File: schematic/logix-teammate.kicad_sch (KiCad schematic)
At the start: 28 parts

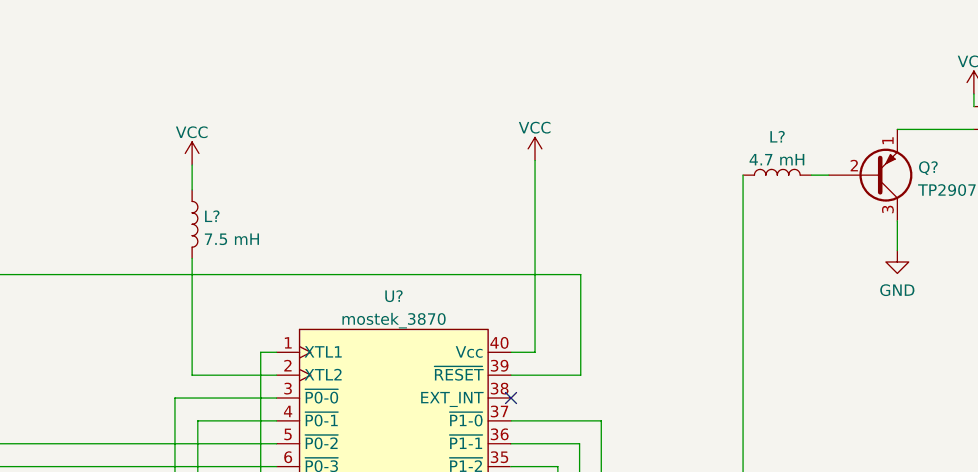
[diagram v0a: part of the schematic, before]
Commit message: corrected resistors
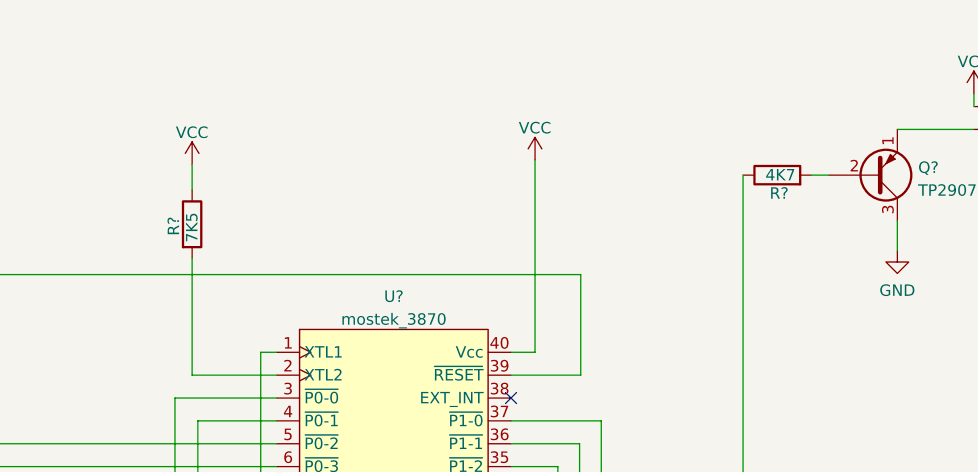
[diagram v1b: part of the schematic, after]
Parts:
- removed L?: 7.5 mH, symbol Device:L
- removed L?: 4.7 mH, symbol Device:L
- added R?: 7K5, symbol Device:R
- added R?: 4K7, symbol Device:R
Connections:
- net VCC: now also R?.1
- net at Q?.2 (B): now also R?.2
- net at U?.2 (XTL2): now also R?.2
- net at U?.33 (~{P5-0}): now also R?.1
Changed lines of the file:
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@@
     (pin "3")
+  )
+  (symbol (lib_id "Device:R") (at 88.9 37.592 0) (unit 1)
+    (in_bom yes) (on_board yes)
+    (property "Reference" "R?" (id 0) (at 86.868 38.862 90)
+      (effects (font (size 1.27 1.27)) (justify left))
+    )
+    (property "Value" "7K5" (id 1) (at 88.9 39.624 90)
+      (effects (font (size 1.27 1.27)) (justify left))
+    )
+    (property "Footprint" "" (id 2) (at 87.122 37.592 90)
+      (effects (font (size 1.27 1.27)) hide)
+    )
+    (property "Datasheet" "~" (id 3) (at 88.9 37.592 0)
+      (effects (font (size 1.27 1.27)) hide)
+    )
+    (pin "1")
+    (pin "2")
   )
   (symbol (lib_id "Simulation_SPICE:DIODE") (at 28.702 21.336 0) (unit 1)
@@
     (pin "1")
   )
-  (symbol (lib_id "Device:L") (at 88.9 37.592 0) (unit 1)
-    (in_bom yes) (on_board yes) (fields_autoplaced)
-    (property "Reference" "L?" (id 0) (at 90.17 36.7573 0)
-      (effects (font (size 1.27 1.27)) (justify left))
-    )
-    (property "Value" "7.5 mH" (id 1) (at 90.17 39.2942 0)
-      (effects (font (size 1.27 1.27)) (justify left))
-    )
-    (property "Footprint" "" (id 2) (at 88.9 37.592 0)
-      (effects (font (size 1.27 1.27)) hide)
-    )
-    (property "Datasheet" "~" (id 3) (at 88.9 37.592 0)
-      (effects (font (size 1.27 1.27)) hide)
-    )
-    (pin "1")
-    (pin "2")
-  )
-  (symbol (lib_id "Device:L") (at 153.924 32.131 90) (unit 1)
-    (in_bom yes) (on_board yes) (fields_autoplaced)
-    (property "Reference" "L?" (id 0) (at 153.924 27.9232 90))
-    (property "Value" "4.7 mH" (id 1) (at 153.924 30.4601 90))
-    (property "Footprint" "" (id 2) (at 153.924 32.131 0)
+  (symbol (lib_id "Device:R") (at 153.924 32.131 90) (unit 1)
+    (in_bom yes) (on_board yes)
+    (property "Reference" "R?" (id 0) (at 155.194 34.163 90)
+      (effects (font (size 1.27 1.27)) (justify left))
+    )
+    (property "Value" "4K7" (id 1) (at 155.956 32.131 90)
+      (effects (font (size 1.27 1.27)) (justify left))
+    )
+    (property "Footprint" "" (id 2) (at 153.924 33.909 90)
       (effects (font (size 1.27 1.27)) hide)
     )
@@
       (reference "D?") (unit 1) (value "LED3") (footprint "")
     )
-    (path "/b9464cb5-be60-4318-8cf9-72da0420fd2d"
-      (reference "L?") (unit 1) (value "7.5 mH") (footprint "")
-    )
-    (path "/c63b8724-5fa8-402a-9aaf-6c3f5c788b0e"
-      (reference "L?") (unit 1) (value "4.7 mH") (footprint "")
-    )
     (path "/d2d8d5bc-d157-4dc7-8a38-0eb37d571cc5"
       (reference "LS?") (unit 1) (value "8Ω") (footprint "")
@@
       (reference "R?") (unit 1) (value "1K5") (footprint "")
     )
+    (path "/3f472c77-a5d2-4b6b-9823-a0f6ca014294"
+      (reference "R?") (unit 1) (value "7K5") (footprint "")
+    )
     (path "/4e283cb3-1a3a-4878-86b7-4bf04f7ee0aa"
       (reference "R?") (unit 1) (value "1K5") (footprint "")
@@
       (reference "R?") (unit 1) (value "1K") (footprint "")
     )
+    (path "/cf9a9387-64b3-4fb2-b3b7-204c4f9a1e23"
+      (reference "R?") (unit 1) (value "4K7") (footprint "")
+    )
     (path "/d844314d-080e-4756-9dbe-bc6b67245e8d"

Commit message: update schematics
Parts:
- gave numbers to parts that had none: 28
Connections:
- net VCC: now also U2.18 (VCC)
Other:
- sheet TEAMMATE Keypad renamed Keypad

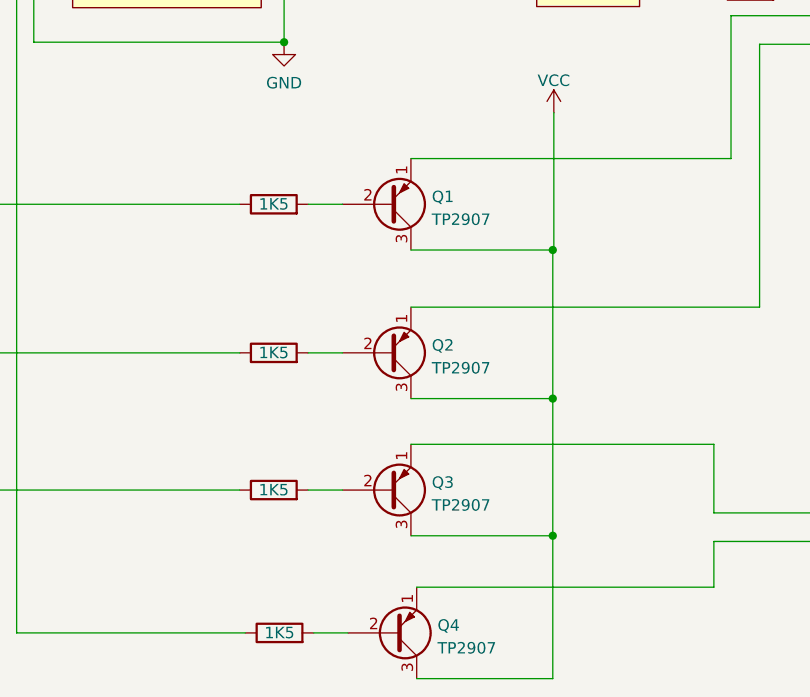
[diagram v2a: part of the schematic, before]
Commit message: corrected transitor polarity
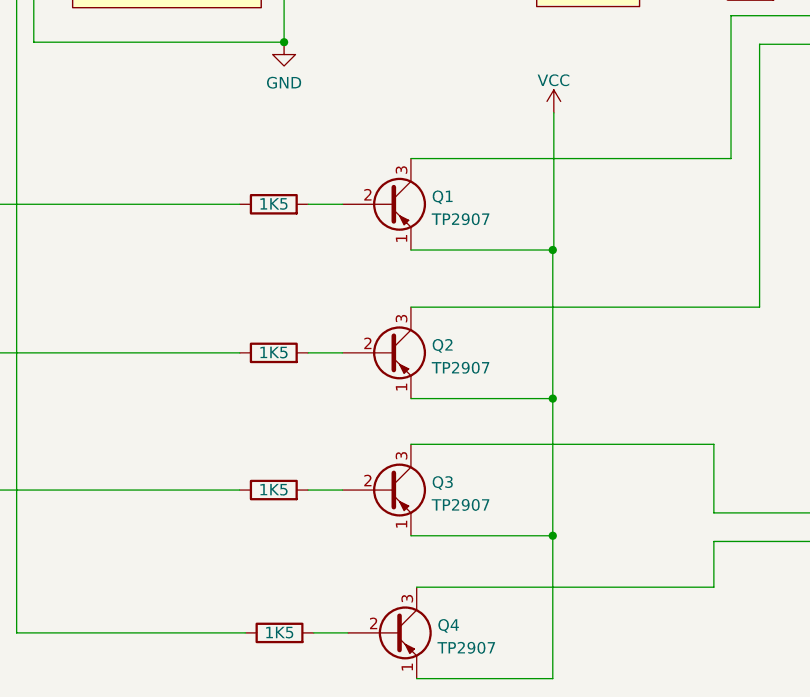
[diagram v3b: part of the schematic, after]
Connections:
- net LED Array/A1: now also Q2.3 (C); no longer Q2.1 (E)
- net LED Array/A2: now also Q1.3 (C); no longer Q1.1 (E)
- net VCC: now also Q1.1 (E), Q2.1 (E), Q3.1 (E), Q4.1 (E); no longer Q1.3 (C), Q2.3 (C), Q3.3 (C), Q4.3 (C)
- net at U4.14 (CA): now also Q4.3 (C); no longer Q4.1 (E)
- net at U3.3 (CA): now also Q3.3 (C); no longer Q3.1 (E)
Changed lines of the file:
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@@
     (pin "2")
   )
-  (symbol (lib_id "Transistor_BJT:2N3906") (at 136.525 171.45 0) (mirror x) (unit 1)
+  (symbol (lib_id "Transistor_BJT:2N3906") (at 136.525 171.45 0) (unit 1)
     (in_bom yes) (on_board yes) (fields_autoplaced)
     (property "Reference" "Q4" (id 0) (at 141.3764 170.6153 0)
@@
       (effects (font (size 1.27 1.27)) (justify left))
     )
-    (property "Footprint" "Package_TO_SOT_THT:TO-92_Inline" (id 2) (at 141.605 169.545 0)
+    (property "Footprint" "Package_TO_SOT_THT:TO-92_Inline" (id 2) (at 141.605 173.355 0)
       (effects (font (size 1.27 1.27) italic) (justify left) hide)
     )
@@
     (pin "2")
   )
-  (symbol (lib_id "Transistor_BJT:2N3906") (at 135.89 140.335 0) (mirror x) (unit 1)
+  (symbol (lib_id "Transistor_BJT:2N3906") (at 135.89 140.335 0) (unit 1)
     (in_bom yes) (on_board yes) (fields_autoplaced)
     (property "Reference" "Q2" (id 0) (at 140.7414 139.5003 0)
@@
       (effects (font (size 1.27 1.27)) (justify left))
     )
-    (property "Footprint" "Package_TO_SOT_THT:TO-92_Inline" (id 2) (at 140.97 138.43 0)
+    (property "Footprint" "Package_TO_SOT_THT:TO-92_Inline" (id 2) (at 140.97 142.24 0)
       (effects (font (size 1.27 1.27) italic) (justify left) hide)
     )
@@
     (pin "9")
   )
-  (symbol (lib_id "Transistor_BJT:2N3906") (at 135.89 123.825 0) (mirror x) (unit 1)
+  (symbol (lib_id "Transistor_BJT:2N3906") (at 135.89 123.825 0) (unit 1)
     (in_bom yes) (on_board yes) (fields_autoplaced)
     (property "Reference" "Q1" (id 0) (at 140.7414 122.9903 0)
@@
       (effects (font (size 1.27 1.27)) (justify left))
     )
-    (property "Footprint" "Package_TO_SOT_THT:TO-92_Inline" (id 2) (at 140.97 121.92 0)
+    (property "Footprint" "Package_TO_SOT_THT:TO-92_Inline" (id 2) (at 140.97 125.73 0)
       (effects (font (size 1.27 1.27) italic) (justify left) hide)
     )
@@
     (pin "2")
   )
-  (symbol (lib_id "Transistor_BJT:2N3906") (at 135.89 155.575 0) (mirror x) (unit 1)
+  (symbol (lib_id "Transistor_BJT:2N3906") (at 135.89 155.575 0) (unit 1)
     (in_bom yes) (on_board yes) (fields_autoplaced)
     (property "Reference" "Q3" (id 0) (at 140.7414 154.7403 0)
@@
       (effects (font (size 1.27 1.27)) (justify left))
     )
-    (property "Footprint" "Package_TO_SOT_THT:TO-92_Inline" (id 2) (at 140.97 153.67 0)
+    (property "Footprint" "Package_TO_SOT_THT:TO-92_Inline" (id 2) (at 140.97 157.48 0)
       (effects (font (size 1.27 1.27) italic) (justify left) hide)
     )
